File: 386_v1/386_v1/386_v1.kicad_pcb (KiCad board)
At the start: 2 copper layers, 70 parts, among them U1 74LVC1G17GW, U2 74LVC1G17GW, U3 i386SX, U7 Conn_02x32_Odd_Even, U7A1 Conn_02x32_Odd_Even, U8 Conn_02x32_Odd_Even, U8A1 Conn_02x32_Odd_Even

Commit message: update
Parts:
- removed U7A1, U8A1: Conn_02x32_Odd_Even, Connector_PinHeader_2.54mm:PinHeader_2x32_P2.54mm_Vertical
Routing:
- net +3V3: track 17.6 -> 63.5 mm
- net /F_~BLE~_O: track 16.2 -> 8.83 mm
- net /F_D14_IO: track 16.2 -> 8.81 mm
- net /F_D10_IO: track 16.2 -> 8.80 mm
- net /F_A19_O: track 16.2 -> 8.80 mm
- net /12: track 7.37 -> 0.00 mm
- net /F_RST_I: track 63.7 -> 56.4 mm
- net /F_A2_O: track 14.2 -> 6.85 mm
- net /F_D7_IO: track 14.2 -> 6.87 mm
- net /F_A12_O: track 14.2 -> 6.87 mm
- net /F_A3_O: track 16.2 -> 8.81 mm
- net /F_D6_IO: track 16.2 -> 8.81 mm
- net /F_A13_O: track 16.2 -> 8.81 mm
- net /F_~READY~_I: track 43.4 -> 36.0 mm
- net /F_~FLT~_I: track 64.6 -> 57.2 mm
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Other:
- board outline added: 69 x 84 mm

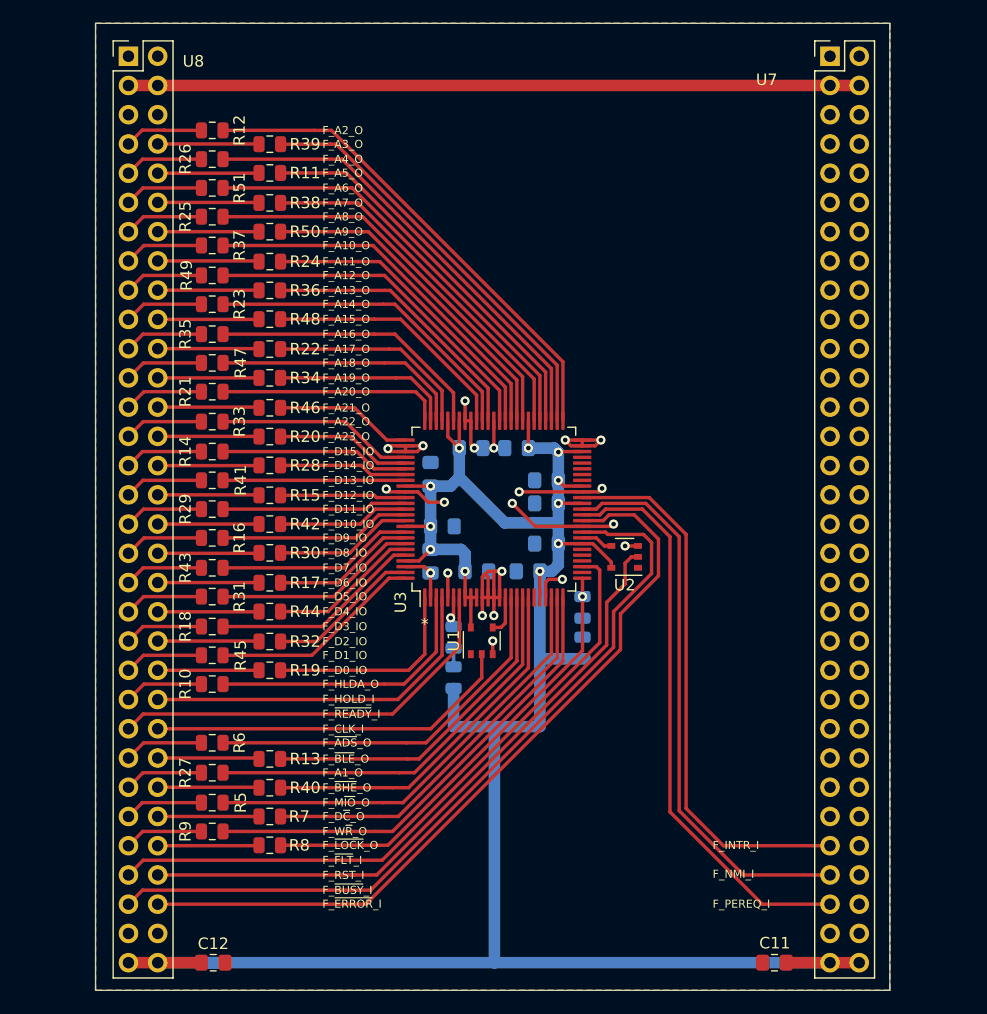
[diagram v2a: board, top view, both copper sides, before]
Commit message: update schematic, use active level shifters
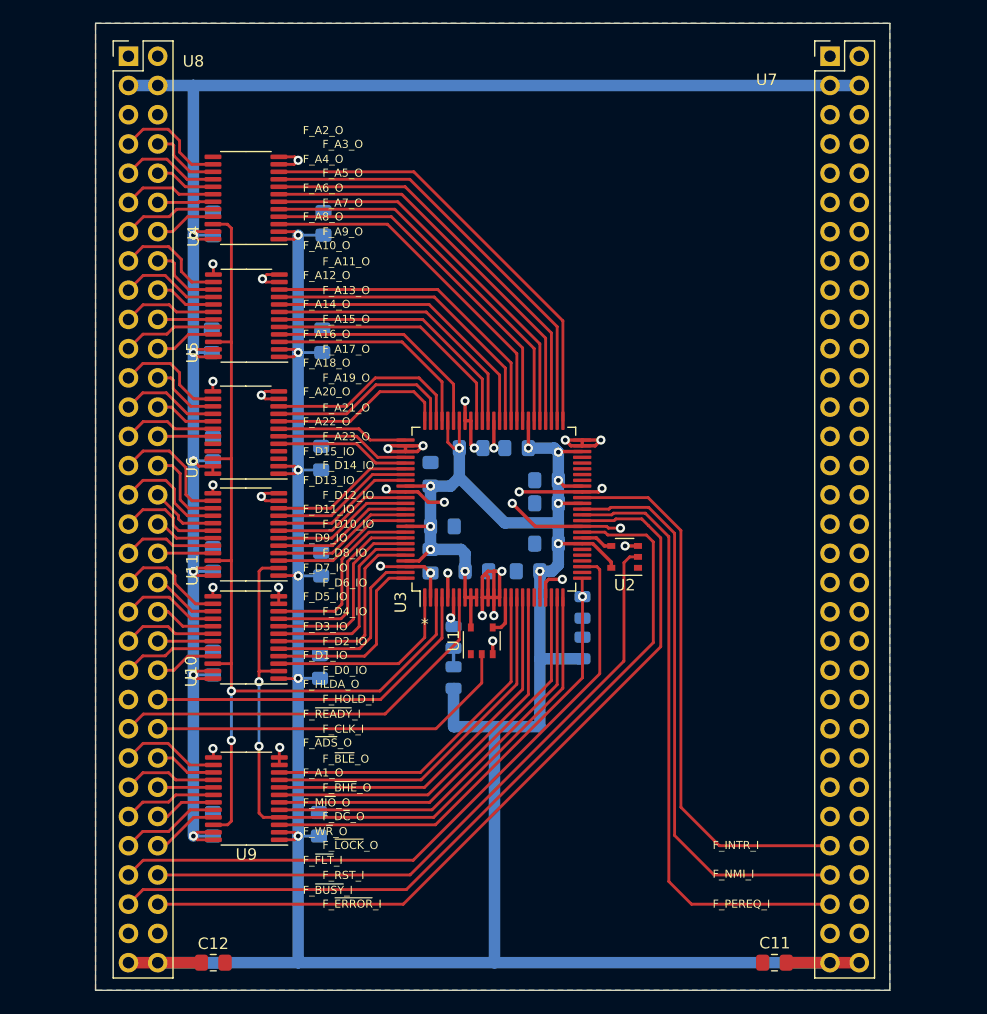
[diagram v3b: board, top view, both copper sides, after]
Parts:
- removed R10, R11, R12, R13, R14, R15, R16, R17, R18, R19, R20, R21, R22, R23, R24, R25, R26, R27, R28, R29, R30, R31, R32, R33, R34, R35, R36, R37, R38, R39, R40, R41, R42, R43, R44, R45, R46, R47, R48, R49, R5, R50, R51, R6, R7, R8, R9: 120, Resistor_SMD:R_0805_2012Metric
- added C13: 100n, Capacitor_SMD:C_0805_2012Metric_Pad1.15x1.40mm_HandSolder, B.Cu at (39.2, 42.5)
- added C14: 100n, Capacitor_SMD:C_0805_2012Metric_Pad1.15x1.40mm_HandSolder, B.Cu at (39.1, 52.7)
- added C15: 100n, Capacitor_SMD:C_0805_2012Metric_Pad1.15x1.40mm_HandSolder, B.Cu at (39.2, 62.1)
- added C16: 100n, Capacitor_SMD:C_0805_2012Metric_Pad1.15x1.40mm_HandSolder, B.Cu at (39.2, 71.7)
- added C17: 100n, Capacitor_SMD:C_0805_2012Metric_Pad1.15x1.40mm_HandSolder, B.Cu at (39.2, 94.7)
- added C18: 100n, Capacitor_SMD:C_0805_2012Metric_Pad1.15x1.40mm_HandSolder, B.Cu at (39.2, 80.7)
- added C19: 100n, Capacitor_SMD:C_0805_2012Metric_Pad1.15x1.40mm_HandSolder, B.Cu at (48.5, 81.0)
- added C20: 100n, Capacitor_SMD:C_0805_2012Metric_Pad1.15x1.40mm_HandSolder, B.Cu at (48.4, 94.7)
- added C21: 100n, Capacitor_SMD:C_0805_2012Metric_Pad1.15x1.40mm_HandSolder, B.Cu at (48.6, 62.9)
- added C22: 100n, Capacitor_SMD:C_0805_2012Metric_Pad1.15x1.40mm_HandSolder, B.Cu at (48.6, 72.1)
- added C23: 100n, Capacitor_SMD:C_0805_2012Metric_Pad1.15x1.40mm_HandSolder, B.Cu at (48.8, 42.5)
- added C24: 100n, Capacitor_SMD:C_0805_2012Metric_Pad1.15x1.40mm_HandSolder, B.Cu at (48.7, 52.7)
- added U10: SN74LVC4245A, Package_SO:TSSOP-24_4.4x7.8mm_P0.65mm, F.Cu at (42.0, 78.5)
- added U11: SN74LVC4245A, Package_SO:TSSOP-24_4.4x7.8mm_P0.65mm, F.Cu at (42.0, 69.5)
- added U4: SN74LVC4245A, Package_SO:TSSOP-24_4.4x7.8mm_P0.65mm, F.Cu at (42.1, 40.3)
- added U5: SN74LVC4245A, Package_SO:TSSOP-24_4.4x7.8mm_P0.65mm, F.Cu at (42.1, 50.5)
- added U6: SN74LVC4245A, Package_SO:TSSOP-24_4.4x7.8mm_P0.65mm, F.Cu at (42.0, 60.6)
- added U9: SN74LVC4245A, Package_SO:TSSOP-24_4.4x7.8mm_P0.65mm, F.Cu at (42.1, 92.5)
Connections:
- net Net-(R2-Pad1) renamed /~LOCK~_O
- U3 pad 1: Net-(R19-Pad2) -> /D0
- U3 pad 100: Net-(R45-Pad2) -> /D1
- U3 pad 16: Net-(R6-Pad1) -> /~ADS~_O
- U3 pad 17: Net-(R13-Pad2) -> /~BLE
- U3 pad 18: Net-(R27-Pad2) -> /A1
- U3 pad 19: Net-(R40-Pad2) -> /~BHE
- U3 pad 23: Net-(R5-Pad1) -> /M~IO~_O
- U3 pad 24: Net-(R7-Pad1) -> /D~C~_O
- U3 pad 25: Net-(R9-Pad1) -> /W~R~_O
- U3 pad 3: Net-(R10-Pad1) -> /HLDA
- U3 pad 51: Net-(R12-Pad2) -> /A2
- U3 pad 52: Net-(R39-Pad2) -> /A3
- U3 pad 53: Net-(R26-Pad2) -> /A4
- U3 pad 54: Net-(R11-Pad2) -> /A5
- U3 pad 55: Net-(R51-Pad2) -> /A6
- U3 pad 56: Net-(R38-Pad2) -> /A7
- U3 pad 58: Net-(R25-Pad2) -> /A8
- U3 pad 59: Net-(R50-Pad2) -> /A9
- U3 pad 60: Net-(R37-Pad2) -> /A10
- U3 pad 61: Net-(R24-Pad2) -> /A11
- U3 pad 62: Net-(R49-Pad2) -> /A12
- U3 pad 64: Net-(R36-Pad2) -> /A13
- U3 pad 65: Net-(R23-Pad2) -> /A14
- U3 pad 66: Net-(R48-Pad2) -> /A15
- U3 pad 70: Net-(R35-Pad2) -> /A16
- U3 pad 72: Net-(R22-Pad2) -> /A17
- U3 pad 73: Net-(R47-Pad2) -> /A18
- U3 pad 74: Net-(R34-Pad2) -> /A19
- U3 pad 75: Net-(R21-Pad2) -> /A20
- U3 pad 76: Net-(R46-Pad2) -> /A21
- U3 pad 79: Net-(R33-Pad2) -> /A22
- U3 pad 80: Net-(R20-Pad2) -> /A23
- U3 pad 81: Net-(R14-Pad2) -> /D15
- U3 pad 82: Net-(R28-Pad2) -> /D14
- U3 pad 83: Net-(R41-Pad2) -> /D13
- U3 pad 86: Net-(R15-Pad2) -> /D12
- U3 pad 87: Net-(R29-Pad2) -> /D11
- U3 pad 88: Net-(R42-Pad2) -> /D10
- U3 pad 89: Net-(R16-Pad2) -> /D9
- U3 pad 90: Net-(R30-Pad2) -> /D8
- U3 pad 92: Net-(R43-Pad2) -> /D7
- U3 pad 93: Net-(R17-Pad2) -> /D6
- U3 pad 94: Net-(R31-Pad2) -> /D5
- U3 pad 95: Net-(R44-Pad2) -> /D4
- U3 pad 96: Net-(R18-Pad2) -> /D3
- U3 pad 99: Net-(R32-Pad2) -> /D2
- U7 pad 10: /10 -> (no net)
- U7 pad 11: /11 -> (no net)
- U7 pad 12: /12 -> (no net)
- U7 pad 13: /13 -> (no net)
- U7 pad 14: /14 -> (no net)
- U7 pad 15: /15 -> (no net)
- U7 pad 16: /16 -> (no net)
- U7 pad 17: /17 -> (no net)
- U7 pad 18: /18 -> (no net)
- U7 pad 19: /19 -> (no net)
- U7 pad 20: /20 -> (no net)
- U7 pad 21: /21 -> (no net)
- U7 pad 22: /22 -> (no net)
- U7 pad 23: /23 -> (no net)
- U7 pad 24: /24 -> (no net)
- U7 pad 25: /25 -> (no net)
- U7 pad 26: /26 -> (no net)
- U7 pad 27: /27 -> (no net)
- U7 pad 28: /28 -> (no net)
- U7 pad 29: /29 -> (no net)
- U7 pad 30: /30 -> (no net)
- U7 pad 31: /31 -> (no net)
- U7 pad 32: /32 -> (no net)
- U7 pad 33: /33 -> (no net)
- U7 pad 34: /34 -> (no net)
- U7 pad 35: /35 -> (no net)
- U7 pad 36: /36 -> (no net)
- U7 pad 37: /37 -> (no net)
- U7 pad 38: /38 -> (no net)
- U7 pad 39: /39 -> (no net)
- U7 pad 40: /40 -> (no net)
- U7 pad 41: /41 -> (no net)
- U7 pad 42: /42 -> (no net)
- U7 pad 43: /43 -> (no net)
- U7 pad 44: /44 -> (no net)
- U7 pad 45: /45 -> (no net)
- U7 pad 46: /46 -> (no net)
- U7 pad 47: /47 -> (no net)
- U7 pad 48: /48 -> (no net)
- U7 pad 49: /49 -> (no net)
- U7 pad 50: /50 -> (no net)
- U7 pad 51: /51 -> (no net)
- U7 pad 52: /52 -> (no net)
- U7 pad 53: /53 -> (no net)
- U7 pad 54: /54 -> (no net)
- U7 pad 56: /56 -> (no net)
- U7 pad 58: /58 -> (no net)
- U7 pad 60: /60 -> (no net)
- U7 pad 7: /7 -> (no net)
- U7 pad 8: /8 -> (no net)
- U7 pad 9: /9 -> (no net)
- U8 pad 45: /F_HLDA_O -> (no net)
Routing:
- net +3V3: track 63.5 -> 159.8 mm, vias 0 -> 6
- net +5V: track 195.9 -> 289.2 mm, vias 11 -> 17
- net /HLDA: track 0.00 -> 84.4 mm, vias 0 -> 2
- net /W~R~_O: track 0.00 -> 63.6 mm, vias 0 -> 2
- net Net-(R12-Pad2): track 43.0 -> 0.00 mm
- net Net-(R9-Pad1): track 41.2 -> 0.00 mm
- net Net-(R26-Pad2): track 40.6 -> 0.00 mm
- net Net-(R5-Pad1): track 38.8 -> 0.00 mm
- net /A2: track 0.00 -> 38.7 mm
- net Net-(R51-Pad2): track 38.2 -> 0.00 mm
- net /A3: track 0.00 -> 37.7 mm
- net Net-(R39-Pad2): track 36.8 -> 0.00 mm
- net /A4: track 0.00 -> 36.6 mm
- net /D~C~_O: track 0.00 -> 36.2 mm
- net Net-(R27-Pad2): track 35.7 -> 0.00 mm
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
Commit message: pcb with buffers
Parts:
- added U12: 74LVC1G17GW, Package_SO:TSOP-5_1.65x3.05mm_P0.95mm, F.Cu at (63.9, 77.3)
- added U13: 74LVC1G17GW, Package_SO:TSOP-5_1.65x3.05mm_P0.95mm, F.Cu at (80.2, 78.0)
- moved C13 9.25 mm to (48.5, 42.5)
- moved C14 9.25 mm to (48.4, 52.7)
- moved C15 9.25 mm to (48.5, 62.1)
- moved C16 9.25 mm to (48.5, 71.7)
- moved C17 9.25 mm to (48.5, 94.7)
- moved C18 9.25 mm to (48.5, 80.7)
- moved C19 9.25 mm to (57.8, 81.0)
- moved C20 9.25 mm to (57.6, 94.7)
- moved C21 9.25 mm to (57.9, 62.9)
- moved C22 9.25 mm to (57.9, 72.1)
- moved C23 9.25 mm to (58.0, 42.5)
- moved C24 9.25 mm to (58.0, 52.7)
- moved U10 9.25 mm to (51.3, 78.5)
- moved U11 9.25 mm to (51.3, 69.5)
- moved U4 9.25 mm to (51.3, 40.3)
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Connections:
- U10 pad 22: /HLDA -> /F_HLDA_O
- U11 pad 22: /HLDA -> /F_HLDA_O
- U3 pad 25: /W~R~_O -> /W~R~_O_RAW
- U3 pad 3: /HLDA -> /HLDA_RAW
- U4 pad 22: /HLDA -> /F_HLDA_O
- U5 pad 22: /HLDA -> /F_HLDA_O
- U6 pad 22: /HLDA -> /F_HLDA_O
- U6 pad 3: (no net) -> GND
- U6 pad 4: (no net) -> GND
- U8 pad 10: /F_A5_O -> /F_~BHE~_O
- U8 pad 11: /F_A6_O -> /F_A4_O
- U8 pad 12: /F_A7_O -> /F_A3_O
- U8 pad 13: /F_A8_O -> /F_A6_O
- U8 pad 14: /F_A9_O -> /F_A5_O
- U8 pad 15: /F_A10_O -> /F_A8_O
- U8 pad 16: /F_A11_O -> /F_A7_O
- U8 pad 17: /F_A12_O -> /F_A10_O
- U8 pad 18: /F_A13_O -> /F_A9_O
- U8 pad 19: /F_A14_O -> /F_A12_O
- U8 pad 20: /F_A15_O -> /F_A11_O
- U8 pad 21: /F_A16_O -> /F_A14_O
- U8 pad 22: /F_A17_O -> /F_A13_O
- U8 pad 23: /F_A18_O -> /F_A16_O
- U8 pad 24: /F_A19_O -> /F_A15_O
- U8 pad 25: /F_A20_O -> /F_A18_O
- U8 pad 26: /F_A21_O -> /F_A17_O
- U8 pad 27: /F_A22_O -> /F_A20_O
- U8 pad 28: /F_A23_O -> /F_A19_O
- U8 pad 29: /F_D15_IO -> /F_A22_O
- U8 pad 30: /F_D14_IO -> /F_A21_O
- U8 pad 31: /F_D13_IO -> /F_HLDA_O
- U8 pad 32: /F_D12_IO -> /F_A23_O
- U8 pad 33: /F_D11_IO -> /F_D14_IO
- U8 pad 34: /F_D10_IO -> /F_D15_IO
- U8 pad 35: /F_D9_IO -> /F_D12_IO
- U8 pad 36: /F_D8_IO -> /F_D13_IO
- U8 pad 37: /F_D7_IO -> /F_D10_IO
- U8 pad 38: /F_D6_IO -> /F_D11_IO
- U8 pad 39: /F_D5_IO -> /F_D8_IO
- U8 pad 40: /F_D4_IO -> /F_D9_IO
- U8 pad 41: /F_D3_IO -> /F_D6_IO
- U8 pad 42: /F_D2_IO -> /F_D7_IO
- U8 pad 43: /F_D1_IO -> /F_D4_IO
- U8 pad 44: /F_D0_IO -> /F_D5_IO
- U8 pad 45: (no net) -> /F_D2_IO
- U8 pad 46: /F_HOLD_I -> /F_D3_IO
- U8 pad 47: /F_~READY~_I -> /F_D0_IO
- U8 pad 48: /F_CLK_I -> /F_D1_IO
- U8 pad 49: /F_~ADS~_O -> /F_~READY~_I
- U8 pad 50: /F_~BLE~_O -> /F_HOLD_I
- U8 pad 51: /F_A1_O -> /F_~ADS~_O
- U8 pad 52: /F_~BHE~_O -> /F_CLK_I
- U8 pad 7: /F_A2_O -> /F_A1_O
- U8 pad 8: /F_A3_O -> /F_~BLE~_O
- U8 pad 9: /F_A4_O -> /F_A2_O
- U9 pad 22: /HLDA -> /F_HLDA_O
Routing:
- net /F_HLDA_O: track 0.00 -> 97.3 mm, vias 0 -> 2
- net /HLDA: track 84.4 -> 0.00 mm, vias 2 -> 0
- net /F_~BLE~_O: track 5.36 -> 65.8 mm, vias 0 -> 1
- net /F_A1_O: track 8.16 -> 68.5 mm, vias 0 -> 1
- net /F_~BHE~_O: track 4.84 -> 64.6 mm, vias 0 -> 1
- net /F_D8_IO: track 4.79 -> 19.7 mm
- net /F_D0_IO: track 5.29 -> 20.2 mm
- net /F_D2_IO: track 4.79 -> 19.7 mm
- net /F_D10_IO: track 5.29 -> 19.2 mm
- net /F_D4_IO: track 5.31 -> 19.2 mm
- net /F_~READY~_I: track 35.6 -> 49.0 mm, vias 0 -> 1
- net /F_HOLD_I: track 30.4 -> 43.5 mm
- net /F_D6_IO: track 5.82 -> 18.7 mm
- net /F_D12_IO: track 5.98 -> 18.7 mm
- net /F_CLK_I: track 32.3 -> 44.7 mm, vias 0 -> 1
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
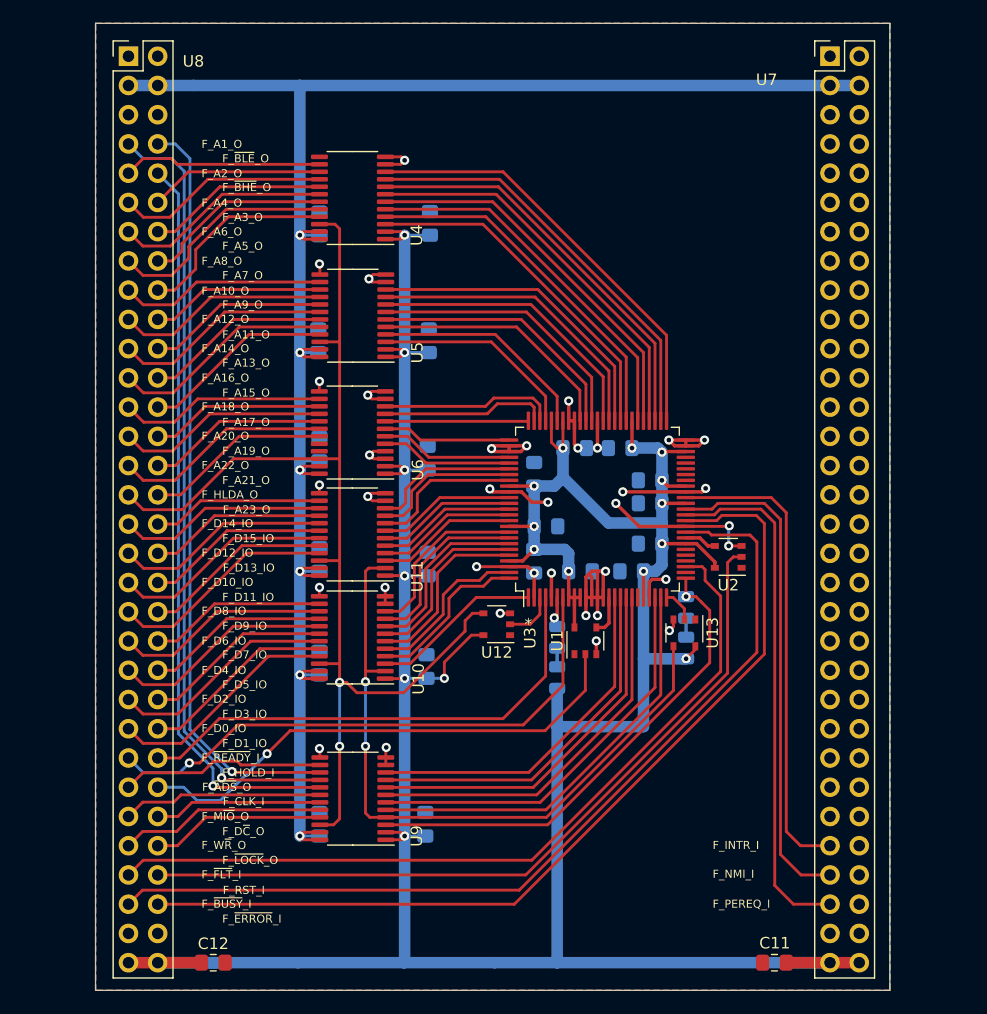
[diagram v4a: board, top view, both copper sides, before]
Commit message: update schematic
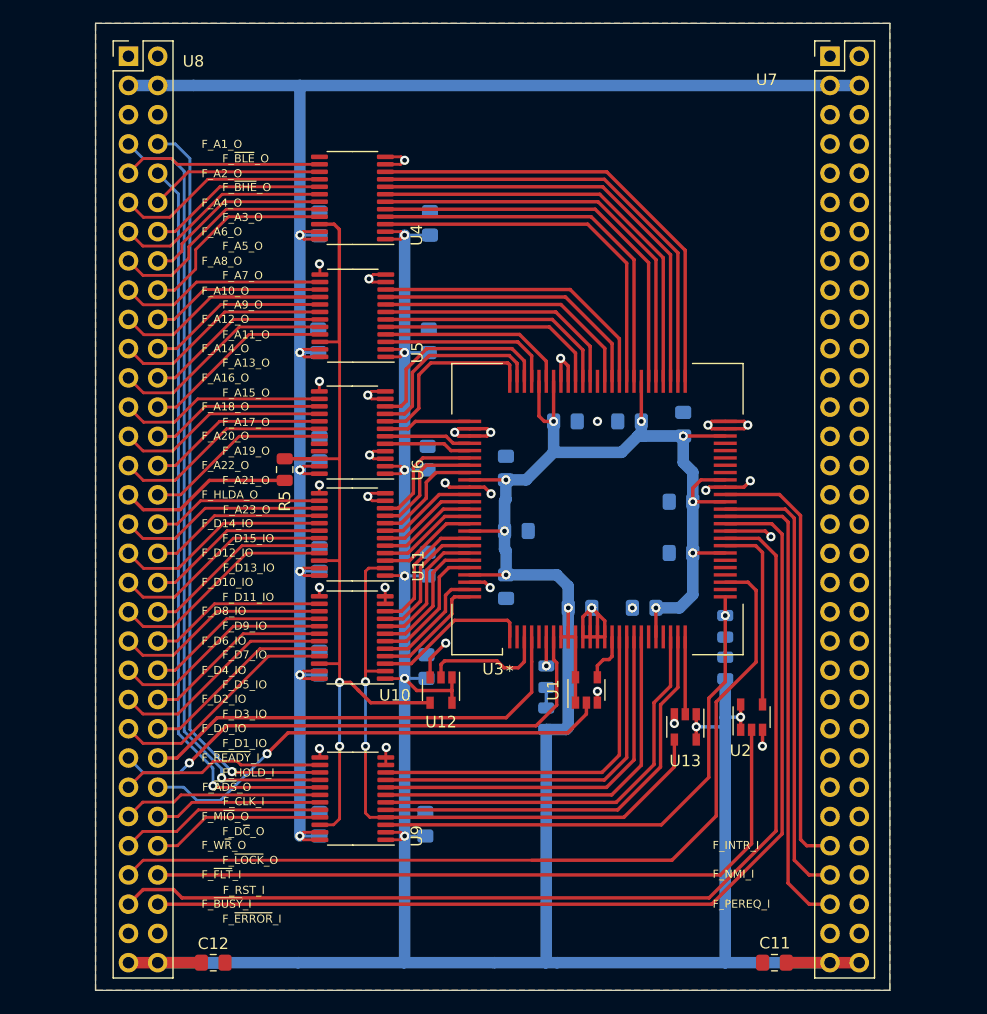
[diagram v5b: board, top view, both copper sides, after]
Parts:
- added R5: 10k, Resistor_SMD:R_0805_2012Metric, F.Cu at (45.4, 63.9)
- U1, U12, U13, U2: value 74LVC1G17GW -> 74AHCT1G126; footprint Package_SO:TSOP-5_1.65x3.05mm_P0.95mm -> Package_TO_SOT_SMD:SOT-23-5
- U3: footprint Package_QFP:LQFP-100_14x14mm_P0.5mm -> 386_v1:QFP-100_25x25_Pitch0.635mm
- moved U2 14.1 mm to (86.0, 85.4), turned to 90 degrees
- moved U13 8.17 mm to (80.2, 86.2)
- moved U12 7.49 mm to (59.0, 83.0), turned to 270 degrees
- moved C5 5.66 mm to (80.0, 59.9), turned to 90 degrees
- moved U1 4.27 mm to (71.6, 83.0)
- moved R1 3.82 mm to (83.7, 81.1)
- moved R2 3.78 mm to (83.7, 77.5)
- moved R3 3.69 mm to (68.2, 85.5)
- moved R4 3.55 mm to (68.2, 81.9)
- moved C2 3.36 mm to (76.7, 75.9)
- moved C9 3.29 mm to (64.7, 74.0)
- moved C1 3.18 mm to (71.1, 75.9)
- moved C3 2.80 mm to (79.9, 71.1)
- moved C4 2.68 mm to (79.9, 66.7)
- moved C10 2.60 mm to (65.6, 69.2)
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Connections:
- U1 pad 1: (no net) -> +5V
- U12 pad 1: (no net) -> +5V
- U13 pad 1: (no net) -> +5V
- U2 pad 1: (no net) -> +5V
- U8 pad 31: /F_HLDA_O -> Net-(R5-Pad2)
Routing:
- net +5V: track 297.9 -> 338.9 mm, vias 19 -> 18
- net GND: track 102.9 -> 76.5 mm, vias 36 -> 30
- net /F_HLDA_O: track 97.3 -> 73.9 mm
- net Net-(R5-Pad2): track 0.00 -> 15.2 mm
- net Net-(U2-Pad4): track 2.81 -> 16.7 mm
- net /F_~BUSY~_I: track 79.8 -> 88.4 mm
- net /F_~ERROR~_I: track 80.3 -> 88.1 mm
- net /F_~FLT~_I: track 70.0 -> 77.2 mm
- net /HLDA_RAW: track 4.42 -> 11.1 mm
- net /F_RST_I: track 67.8 -> 62.6 mm
- net /D1: track 14.5 -> 10.2 mm
- net /D3: track 15.9 -> 11.6 mm
- net /D2: track 14.5 -> 10.3 mm
- net /W~R~_O: track 59.9 -> 55.7 mm
- net /D4: track 15.8 -> 11.7 mm
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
